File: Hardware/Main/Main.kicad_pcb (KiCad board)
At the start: 2 copper layers, 80 x 80 mm, 56 parts, among them CN1 XT30UPB-F, J1 Pinhead_01x02_horizontal, J2 Pinhead_01x02_horizontal, J3 Pinhead_01x02_horizontal, J4 Pinhead_01x02_horizontal, J5 Conn_02x04_Row_Letter_First, U10 Pinhead_1x02H, U11 LM1117IMPX-3_3_NOPB, U12 Pinhead_1x02H, U2 Switch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

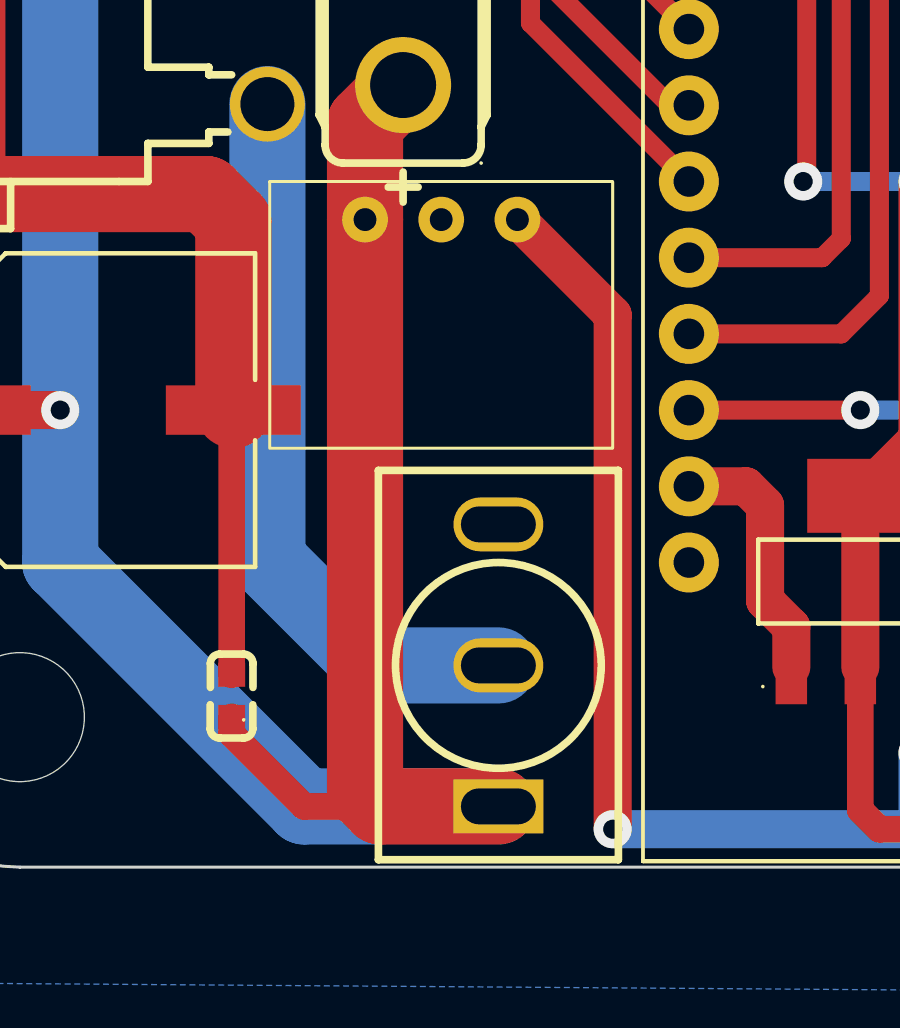
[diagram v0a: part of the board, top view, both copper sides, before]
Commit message: Updated pcb design of main board
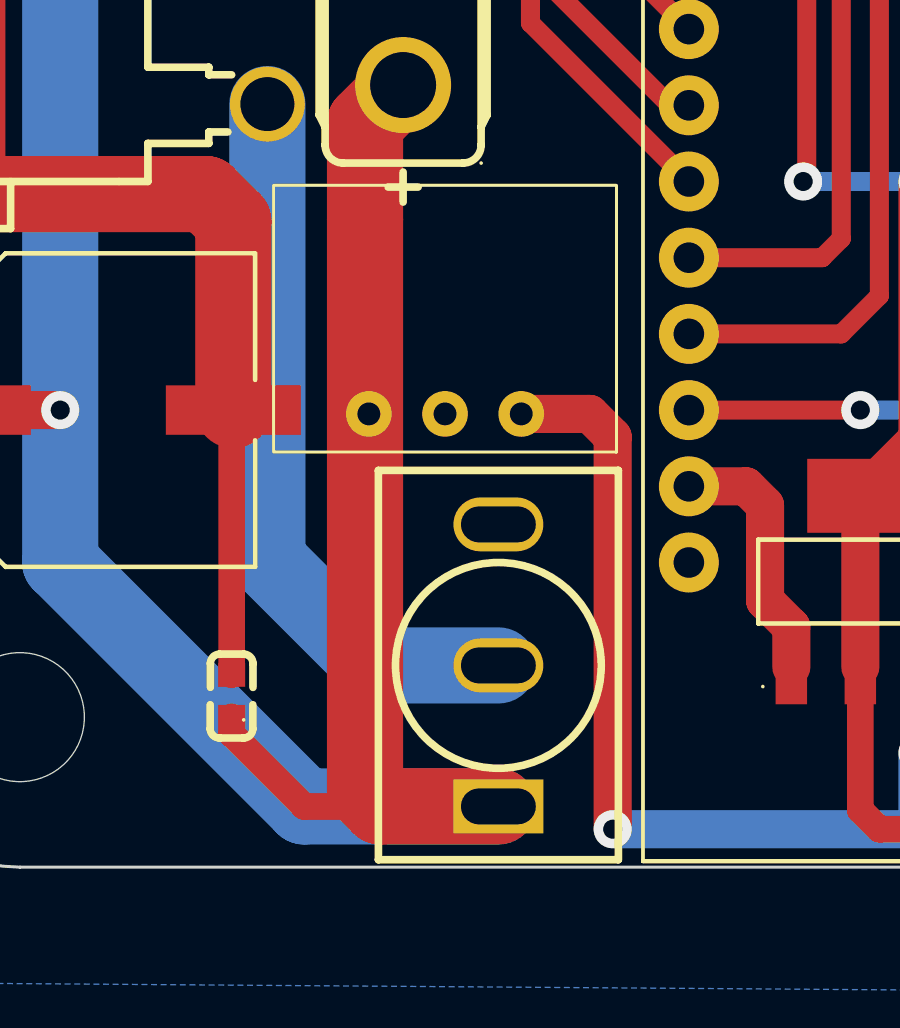
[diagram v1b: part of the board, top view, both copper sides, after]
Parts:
- moved R78K1 6.48 mm to (-20.8, 24.9), turned to 180 degrees
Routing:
- net +5V: track 150.9 -> 145.7 mm
